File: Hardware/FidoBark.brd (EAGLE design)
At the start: 100 x 80 mm, 37 parts, among them T1 BPX81, U3 HM-10

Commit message: sd and ble
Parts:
- moved U$2 97.1 mm to (31.8, 2.54), turned to 90 degrees
- moved U3 90.4 mm to (48.3, 31.8), turned to 180 degrees
- moved J1 14.0 mm to (10.2, 5.08)
- moved JP2 11.4 mm to (26.7, 2.54)
- moved JP1 11.4 mm to (20.3, 2.54)
- moved U$3 11.4 mm to (22.9, 9.53)
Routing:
- net GND: track 28.2 -> 147.1 mm, vias 0 -> 1
- net RX: track 0.00 -> 60.8 mm, vias 0 -> 1
- net 3.3V: track 35.6 -> 94.3 mm, vias 0 -> 1
- net TX: track 0.00 -> 48.1 mm, vias 0 -> 1
- net SCK: track 0.00 -> 32.6 mm
- net MISO: track 0.00 -> 27.4 mm
- net MOSI: track 0.00 -> 15.7 mm
- net MOT_PWMB: track 0.00 -> 15.7 mm
- net SS: track 0.00 -> 12.5 mm
- net MOT_B2: track 0.00 -> 7.30 mm
- net MOT_A2: track 13.3 -> 6.25 mm
- net MOT_B1: track 0.00 -> 6.52 mm
- net MOT_A1: track 11.7 -> 7.03 mm
- net V_BATT: track 22.3 -> 26.0 mm
- net MOT_PWMA: track 10.1 -> 7.81 mm

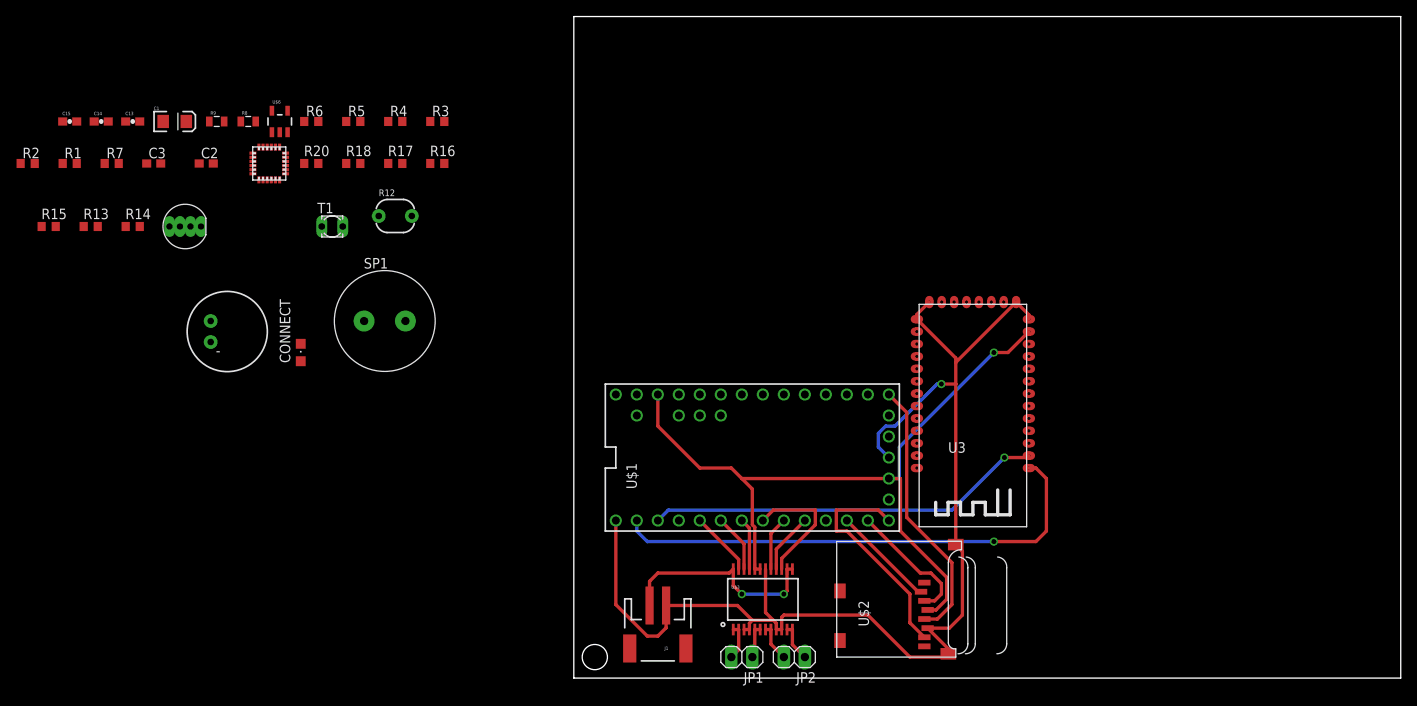
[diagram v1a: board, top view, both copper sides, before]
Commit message: piezo and led
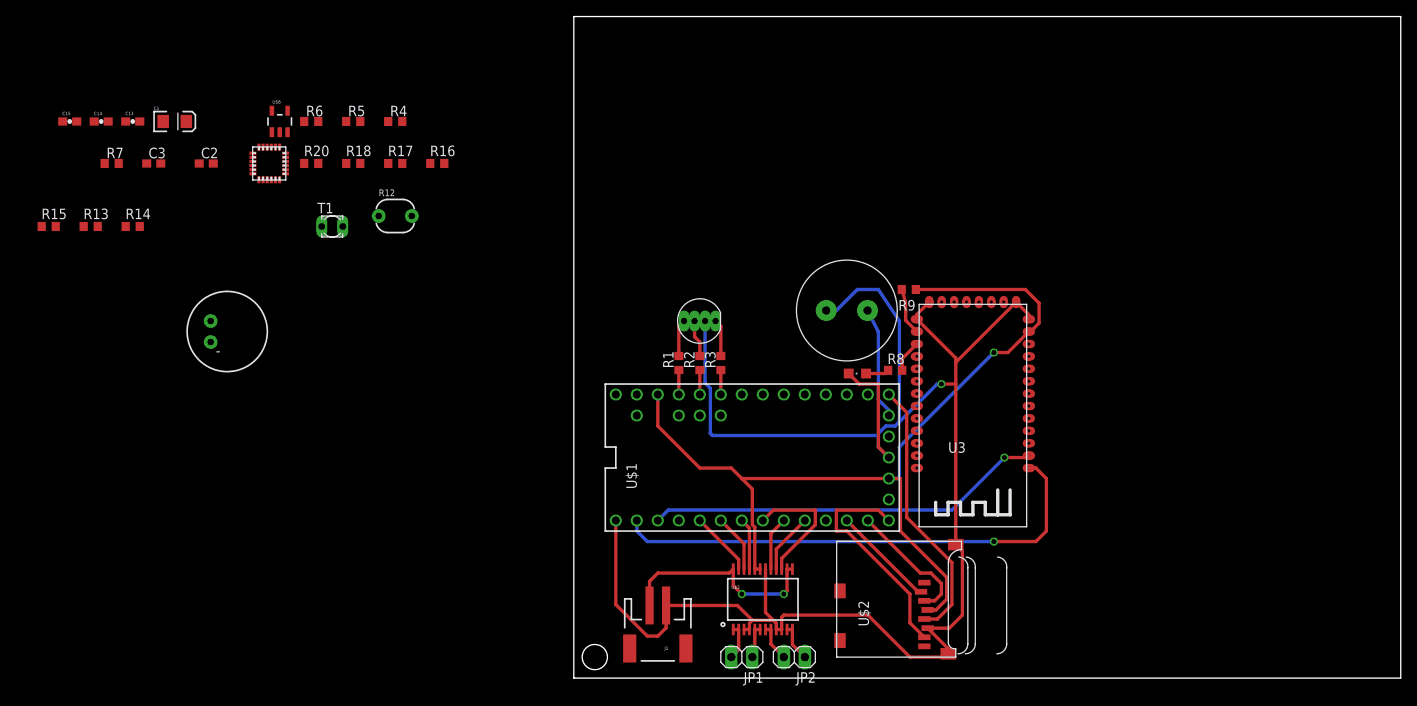
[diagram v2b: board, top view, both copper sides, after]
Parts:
- R8, R9: value 470R -> 470; device SparkFun-Resistors:0805 -> adafruit:R0603
- moved R9 86.1 mm to (40.5, 47.0), turned to 180 degrees
- moved R2 84.8 mm to (15.2, 38.1), turned to 90 degrees
- moved R8 83.8 mm to (38.9, 37.2), turned to 180 degrees
- moved R1 77.5 mm to (12.7, 38.1), turned to 90 degrees
- moved CONNECT 67.4 mm to (34.3, 36.8), turned to 90 degrees
- moved D1 63.3 mm to (15.2, 43.2)
- moved SP1 55.9 mm to (33.0, 44.5), turned to 180 degrees
- moved R3 45.0 mm to (17.8, 38.1), turned to 90 degrees
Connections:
- net 3.3V: now also R9.1; no longer R8.2
- net N$10: now also R8.1; no longer R9.1
- net N$11: now also R9.2; no longer R8.1
- net N$16: now also R8.2; no longer R9.2
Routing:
- net GND: track 147.1 -> 219.1 mm
- net 3.3V: track 94.3 -> 113.9 mm
- net PIEZO: track 0.00 -> 13.5 mm
- net N$11: track 0.00 -> 5.72 mm
- net N$7: track 0.00 -> 4.49 mm
- net N$2: track 0.00 -> 4.49 mm
- net N$6: track 0.00 -> 4.49 mm
- net N$10: track 0.00 -> 3.93 mm
- net LED_R: track 0.00 -> 2.96 mm
- net LED_G: track 0.00 -> 2.96 mm
- net LED_B: track 0.00 -> 2.96 mm
- net N$16: track 0.00 -> 2.83 mm

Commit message: visible light and BLE status LED
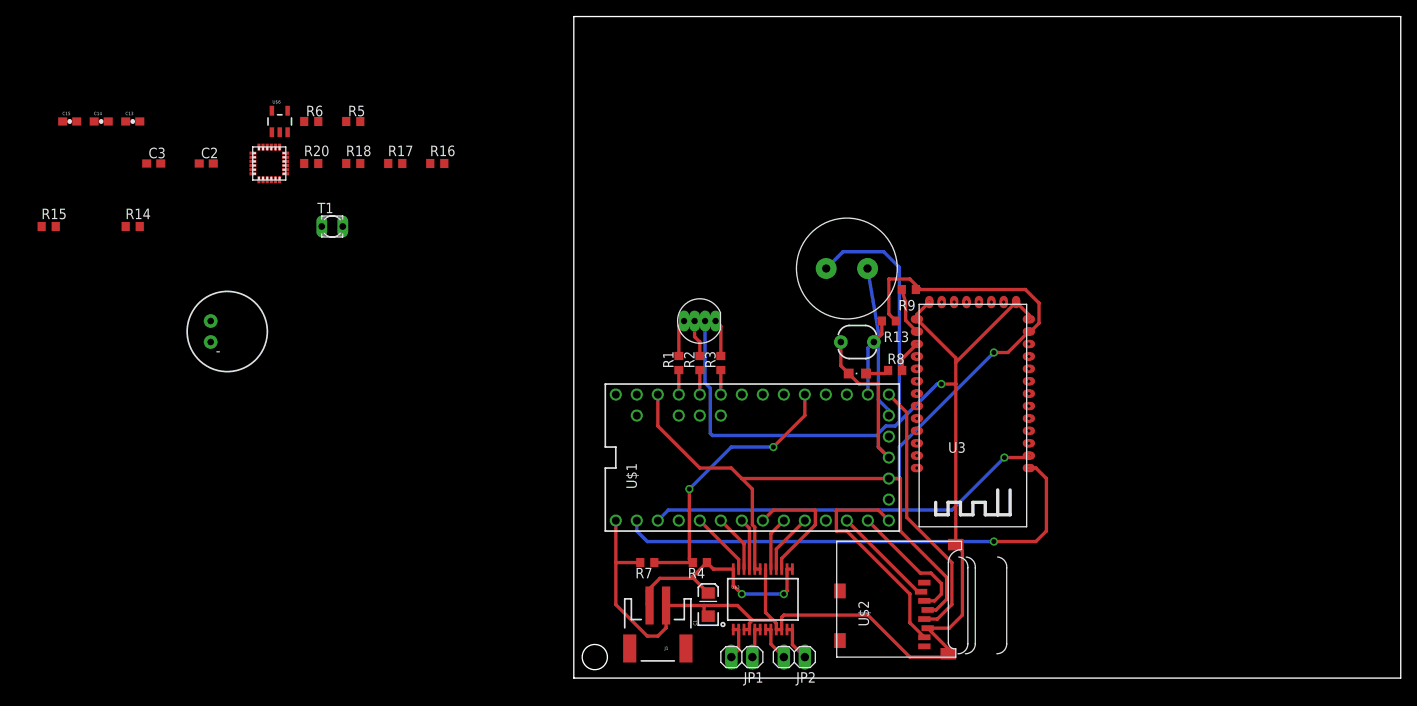
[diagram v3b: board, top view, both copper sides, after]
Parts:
- moved R13 97.2 mm to (38.1, 43.2)
- moved C1 87.0 mm to (16.3, 8.89), turned to 90 degrees
- moved R7 80.8 mm to (8.89, 14.0), turned to 180 degrees
- moved R4 64.8 mm to (15.2, 14.0), turned to 180 degrees
- moved R12 57.9 mm to (34.3, 40.6)
- moved SP1 5.08 mm to (33.0, 49.5)
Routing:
- net ADC_BAT: track 0.00 -> 33.9 mm, vias 0 -> 2
- net GND: track 219.1 -> 232.8 mm
- net 3.3V: track 113.9 -> 123.7 mm
- net ADC_VIS: track 0.00 -> 9.59 mm
- net PIEZO: track 13.5 -> 18.4 mm
- net V_BATT: track 26.0 -> 29.2 mm

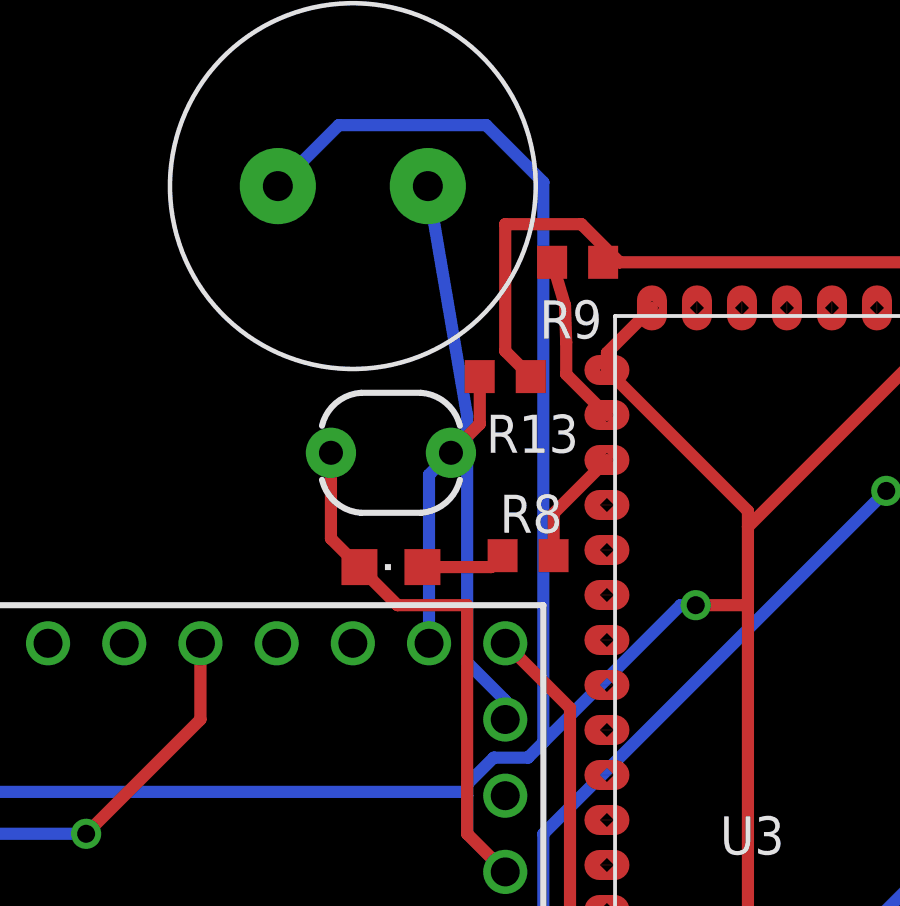
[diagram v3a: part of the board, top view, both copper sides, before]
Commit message: fixed signal crossing
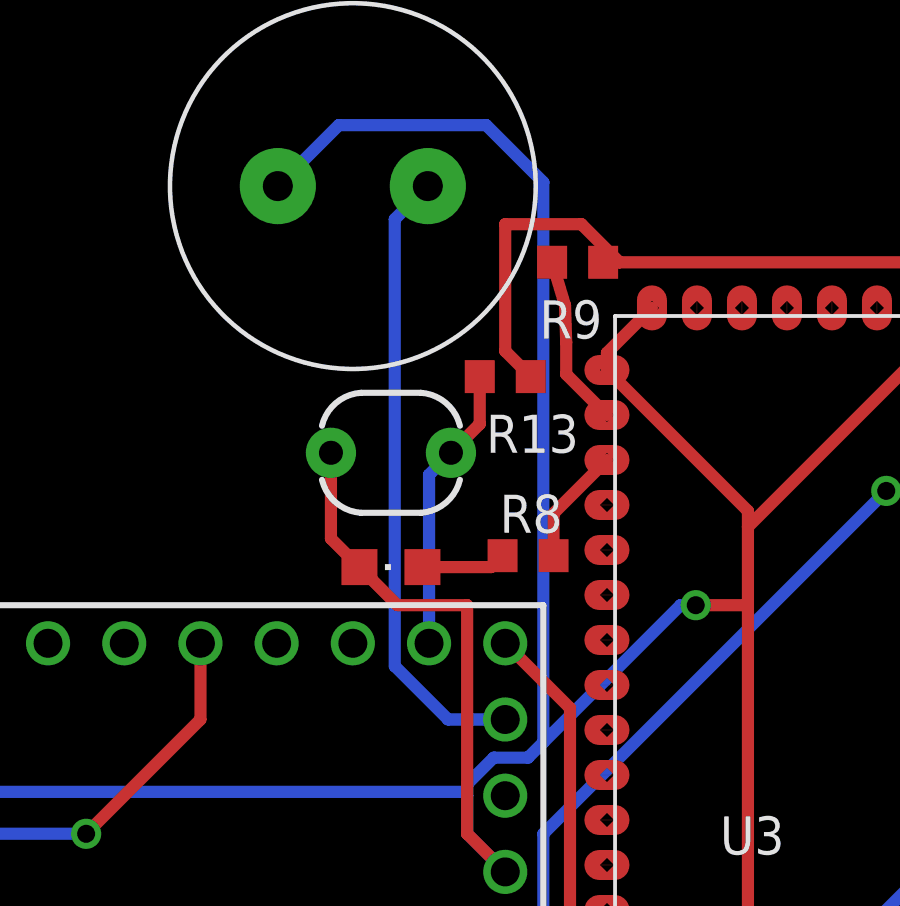
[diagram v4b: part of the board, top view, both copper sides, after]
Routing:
- net PIEZO: track 18.4 -> 20.9 mm
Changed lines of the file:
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@@
 <contactref element="SP1" pad="P$1"/>
 <contactref element="U$1" pad="A14"/>
-<wire x1="38.1" y1="31.75" x2="38.1" y2="32.385" width="0.4064" layer="16"/>
-<wire x1="38.1" y1="32.385" x2="36.83" y2="33.655" width="0.4064" layer="16"/>
-<wire x1="36.83" y1="33.655" x2="36.83" y2="41.87" width="0.4064" layer="16"/>
-<wire x1="36.83" y1="41.87" x2="35.52" y2="49.53" width="0.4064" layer="16"/>
+<wire x1="38.1" y1="31.75" x2="36.195" y2="31.75" width="0.4064" layer="16"/>
+<wire x1="36.195" y1="31.75" x2="34.417" y2="33.528" width="0.4064" layer="16"/>
+<wire x1="34.417" y1="33.528" x2="34.417" y2="48.427" width="0.4064" layer="16"/>
+<wire x1="34.417" y1="48.427" x2="35.52" y2="49.53" width="0.4064" layer="16"/>
 </signal>
 <signal name="ADC_VIS">

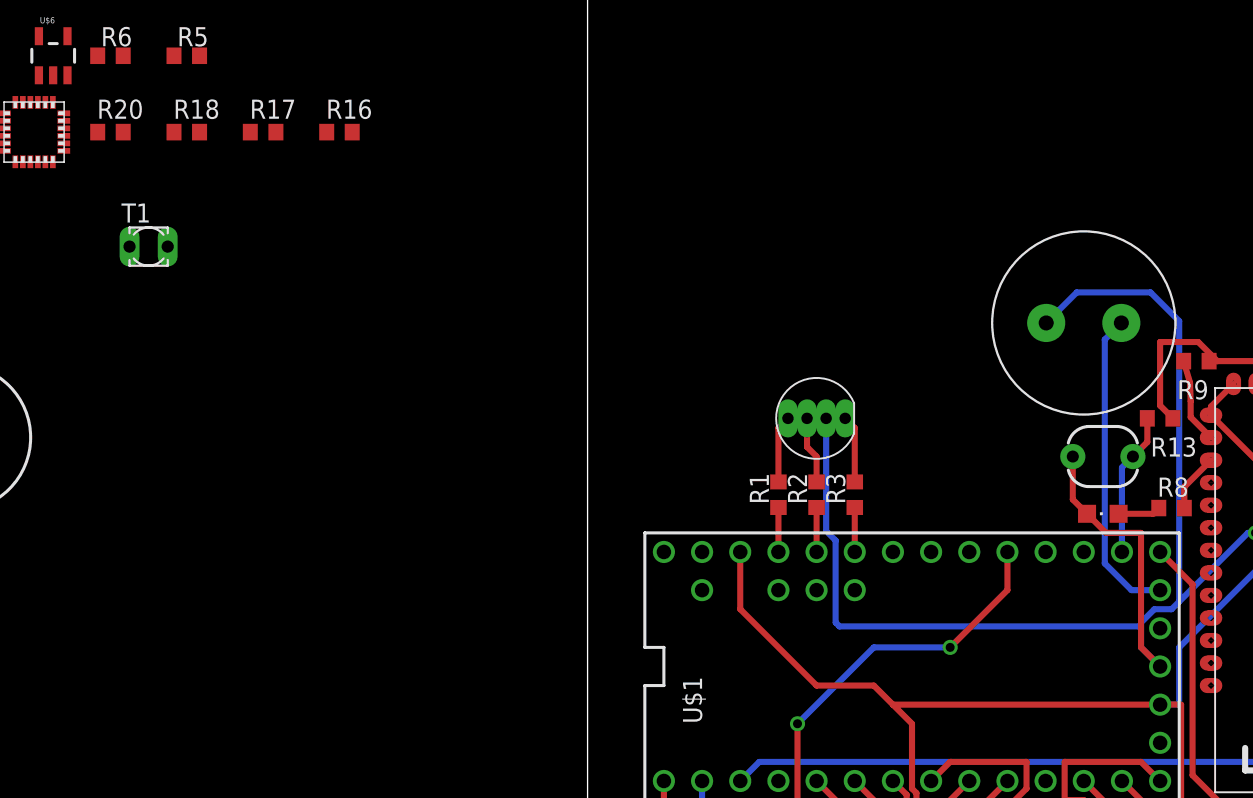
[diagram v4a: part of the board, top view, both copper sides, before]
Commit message: routed IR
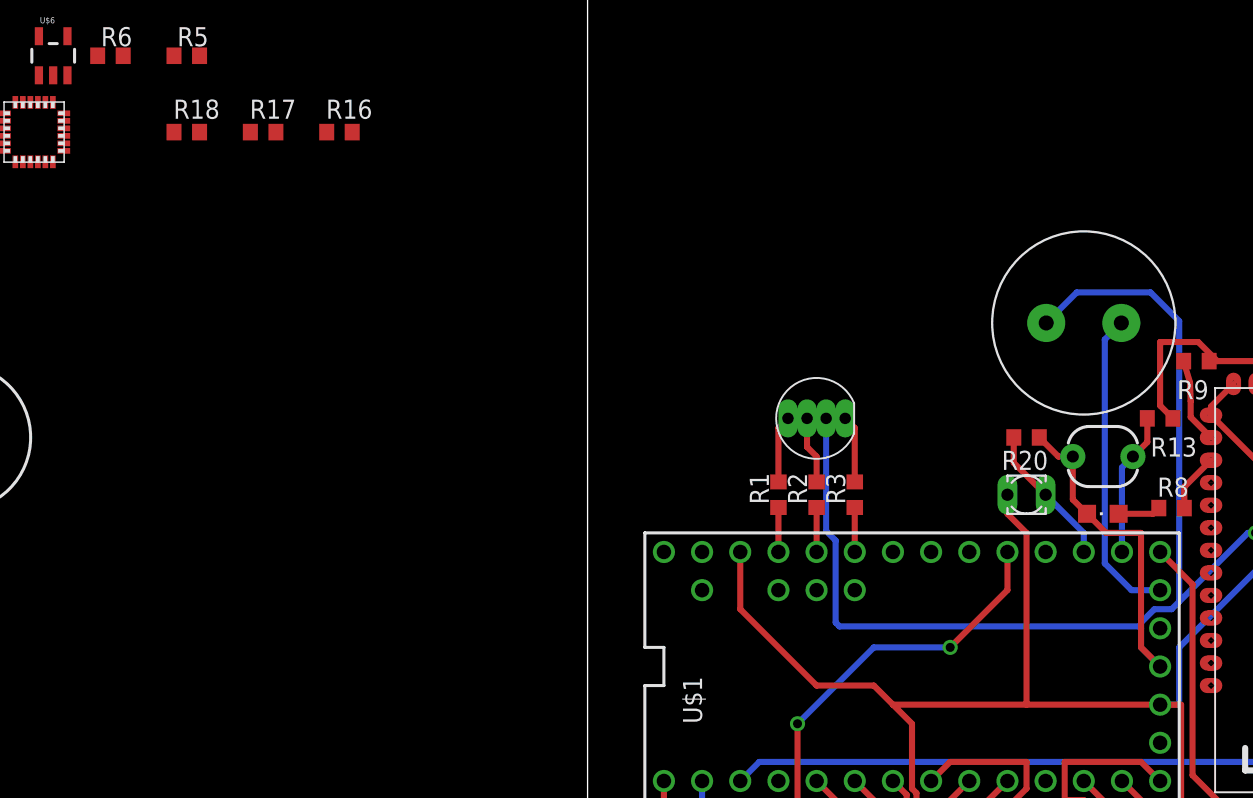
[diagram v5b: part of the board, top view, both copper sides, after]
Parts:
- moved R20 64.3 mm to (29.2, 41.9), turned to 180 degrees
- moved T1 60.7 mm to (29.2, 38.1), turned to 180 degrees
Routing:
- net 3.3V: track 123.7 -> 138.2 mm
- net ADC_IR: track 0.00 -> 9.55 mm
- net GND: track 232.8 -> 235.6 mm
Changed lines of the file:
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@@
 <attribute name="NAME" x="14.605" y="37.465" size="1.27" layer="25" rot="R90"/>
 </element>
-<element name="R20" library="adafruit" package="R0603" value="2k" x="-31.75" y="62.23"/>
+<element name="R20" library="adafruit" package="R0603" value="2k" x="29.21" y="41.91" smashed="yes" rot="R180">
+<attribute name="NAME" x="27.559" y="39.751" size="1.27" layer="25"/>
+</element>
 <element name="R3" library="rcl" package="R0603" value="220" x="17.78" y="38.1" smashed="yes" rot="R90">
 <attribute name="NAME" x="17.145" y="37.465" size="1.27" layer="25" rot="R90"/>
@@
 <element name="R7" library="rcl" package="R0603" value="4.7k" x="8.89" y="13.97" rot="R180"/>
 <element name="SP1" library="adafruit" package="PS12" value="SPEAKER/PS12" x="33.02" y="49.53" smashed="yes" rot="R180"/>
-<element name="T1" library="opto-trans-siemens" package="BPX81" value="BPX81" x="-29.21" y="54.61">
-<attribute name="OC_NEWARK" value="unknown" x="-29.21" y="54.61" size="1.778" layer="27" display="off"/>
-<attribute name="MPN" value="" x="-29.21" y="54.61" size="1.778" layer="27" display="off"/>
-<attribute name="MF" value="" x="-29.21" y="54.61" size="1.778" layer="27" display="off"/>
-<attribute name="OC_FARNELL" value="unknown" x="-29.21" y="54.61" size="1.778" layer="27" display="off"/>
+<element name="T1" library="opto-trans-siemens" package="BPX81" value="BPX81" x="29.21" y="38.1" smashed="yes" rot="R180">
+<attribute name="OC_NEWARK" value="unknown" x="29.21" y="38.1" size="1.778" layer="27" rot="R180" display="off"/>
+<attribute name="MPN" value="" x="29.21" y="38.1" size="1.778" layer="27" rot="R180" display="off"/>
+<attribute name="MF" value="" x="29.21" y="38.1" size="1.778" layer="27" rot="R180" display="off"/>
+<attribute name="OC_FARNELL" value="unknown" x="29.21" y="38.1" size="1.778" layer="27" rot="R180" display="off"/>
 </element>
 <element name="U$1" library="Teensy_3_Series_Board_v1.0" package="TEENSY_3.1+4" value="TEENSY_3.1+4" x="22.86" y="26.67" rot="R90"/>
@@
 <wire x1="15.24" y1="25.4" x2="10.16" y2="30.48" width="0.4064" layer="1"/>
 <wire x1="10.16" y1="30.48" x2="10.16" y2="34.29" width="0.4064" layer="1"/>
-<wire x1="38.1" y1="24.13" x2="20.32" y2="24.13" width="0.4064" layer="1"/>
+<wire x1="38.1" y1="24.13" x2="29.21" y2="24.13" width="0.4064" layer="1"/>
+<wire x1="29.21" y1="24.13" x2="20.32" y2="24.13" width="0.4064" layer="1"/>
 <wire x1="42.79" y1="8.24" x2="43.8" y2="8.24" width="0.4064" layer="1"/>
 <wire x1="43.8" y1="8.24" x2="45.085" y2="9.525" width="0.4064" layer="1"/>
@@
 <wire x1="38.1" y1="48.26" x2="40.64" y2="48.26" width="0.4064" layer="1"/>
 <wire x1="40.64" y1="48.26" x2="41.91" y2="46.99" width="0.4064" layer="1"/>
+<wire x1="27.94" y1="38.1" x2="27.94" y2="36.83" width="0.4064" layer="1"/>
+<wire x1="27.94" y1="36.83" x2="29.21" y2="35.56" width="0.4064" layer="1"/>
+<wire x1="29.21" y1="35.56" x2="29.21" y2="24.13" width="0.4064" layer="1"/>
 <wire x1="-25.82" y1="67.31" x2="-15.66" y2="62.23" width="0" layer="19" extent="1-1"/>
 <wire x1="-30.9" y1="67.31" x2="-25.82" y2="67.31" width="0" layer="19" extent="1-1"/>
@@
 <wire x1="-37.58" y1="60.255" x2="-38.805" y2="62.48" width="0" layer="19" extent="1-1"/>
 <wire x1="-34.855" y1="60.98" x2="-37.58" y2="60.255" width="0" layer="19" extent="1-1"/>
-<wire x1="-27.94" y1="54.61" x2="-34.855" y2="60.98" width="0" layer="19" extent="1-1"/>
 <wire x1="-52.49" y1="54.61" x2="-38.805" y2="62.48" width="0" layer="19" extent="1-1"/>
 <wire x1="10.16" y1="34.29" x2="-15.66" y2="62.23" width="0" layer="19" extent="1-1"/>
@@
 <wire x1="32.29" y1="40.64" x2="32.29" y2="37.78" width="0.4064" layer="1"/>
 <wire x1="32.29" y1="37.78" x2="33.24" y2="36.83" width="0.4064" layer="1"/>
-<wire x1="-32.6" y1="62.23" x2="-22.44" y2="62.23" width="0" layer="19" extent="1-1"/>
-<wire x1="-34.855" y1="61.98" x2="-32.6" y2="62.23" width="0" layer="19" extent="1-1"/>
+<wire x1="30.06" y1="41.91" x2="31.33" y2="40.64" width="0.4064" layer="1"/>
+<wire x1="31.33" y1="40.64" x2="32.29" y2="40.64" width="0.4064" layer="1"/>
+<wire x1="-34.855" y1="61.98" x2="-22.44" y2="62.23" width="0" layer="19" extent="1-1"/>
 <wire x1="-34.855" y1="62.98" x2="-34.855" y2="61.98" width="0" layer="19" extent="1-1"/>
 <wire x1="-34.855" y1="63.48" x2="-34.855" y2="62.98" width="0" layer="19" extent="1-1"/>
@@
 <contactref element="R20" pad="2"/>
 <contactref element="U$1" pad="15/A1"/>
-<wire x1="-30.48" y1="54.61" x2="-30.9" y2="62.23" width="0" layer="19" extent="1-1"/>
-<wire x1="33.02" y1="34.29" x2="-30.48" y2="54.61" width="0" layer="19" extent="1-1"/>
+<wire x1="33.02" y1="34.29" x2="33.02" y2="35.56" width="0.4064" layer="16"/>
+<wire x1="33.02" y1="35.56" x2="30.48" y2="38.1" width="0.4064" layer="16"/>
+<wire x1="30.48" y1="38.1" x2="28.36" y2="40.22" width="0.4064" layer="1"/>
+<wire x1="28.36" y1="40.22" x2="28.36" y2="41.91" width="0.4064" layer="1"/>
 </signal>
 <signal name="N$28">
